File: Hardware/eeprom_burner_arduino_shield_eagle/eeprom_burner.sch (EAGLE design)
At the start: 5 parts, among them IC2 74LS595N, IC3 74LS595N

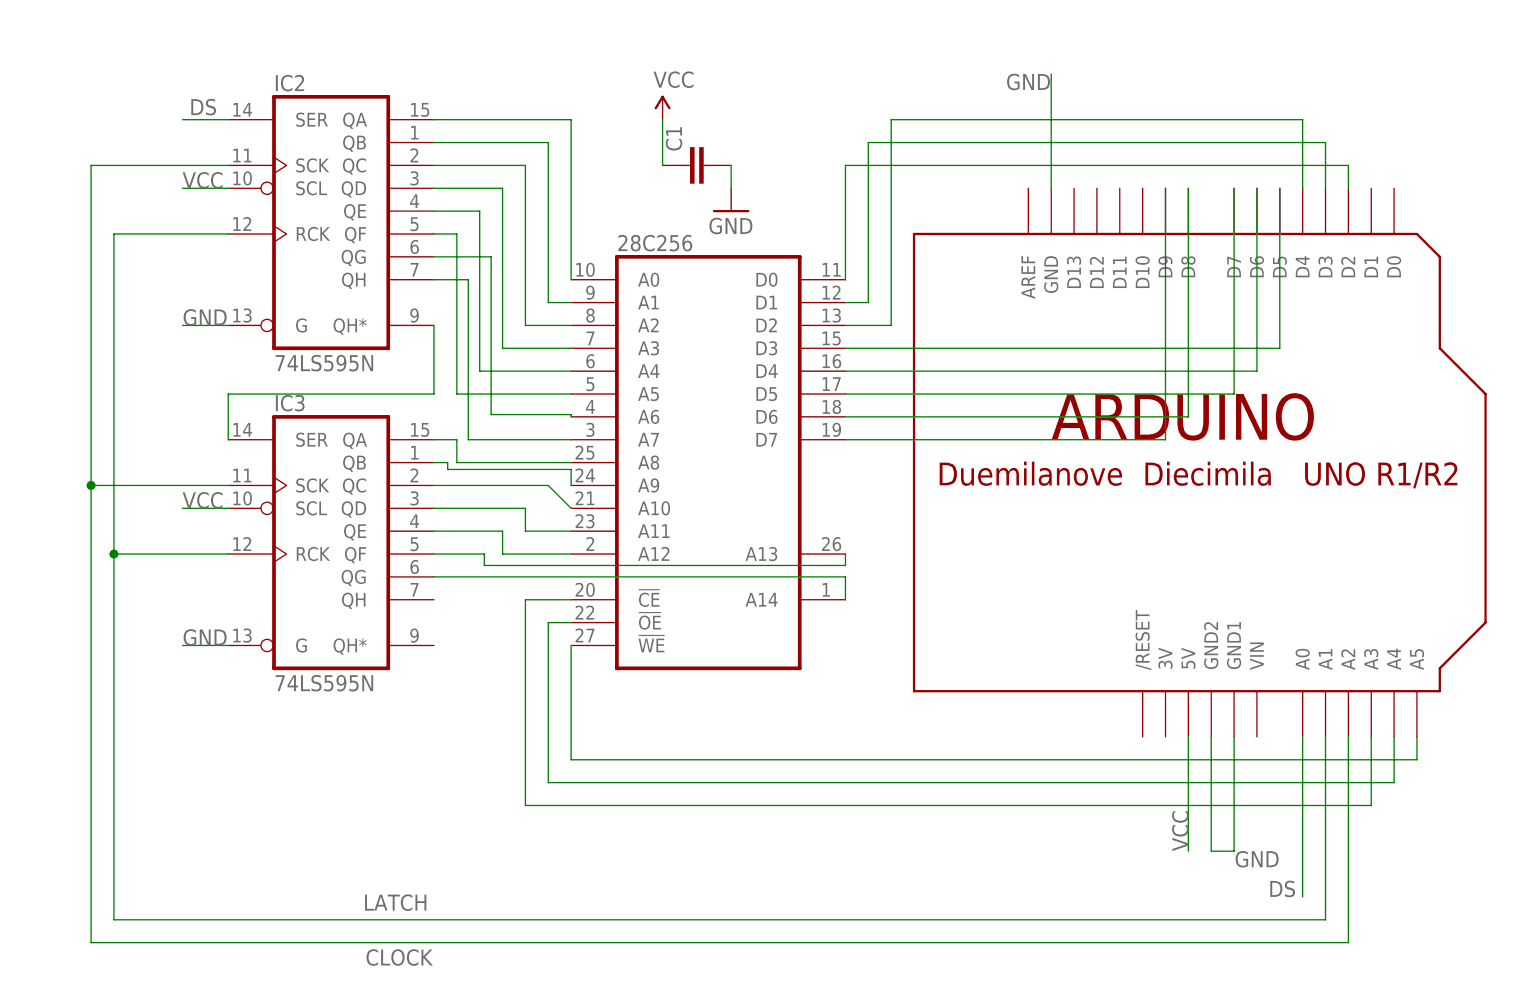
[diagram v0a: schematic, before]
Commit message: Python CLI, Paged Write, Unlocker
Fleshed out python command line interface
Added paged write and unlock functions
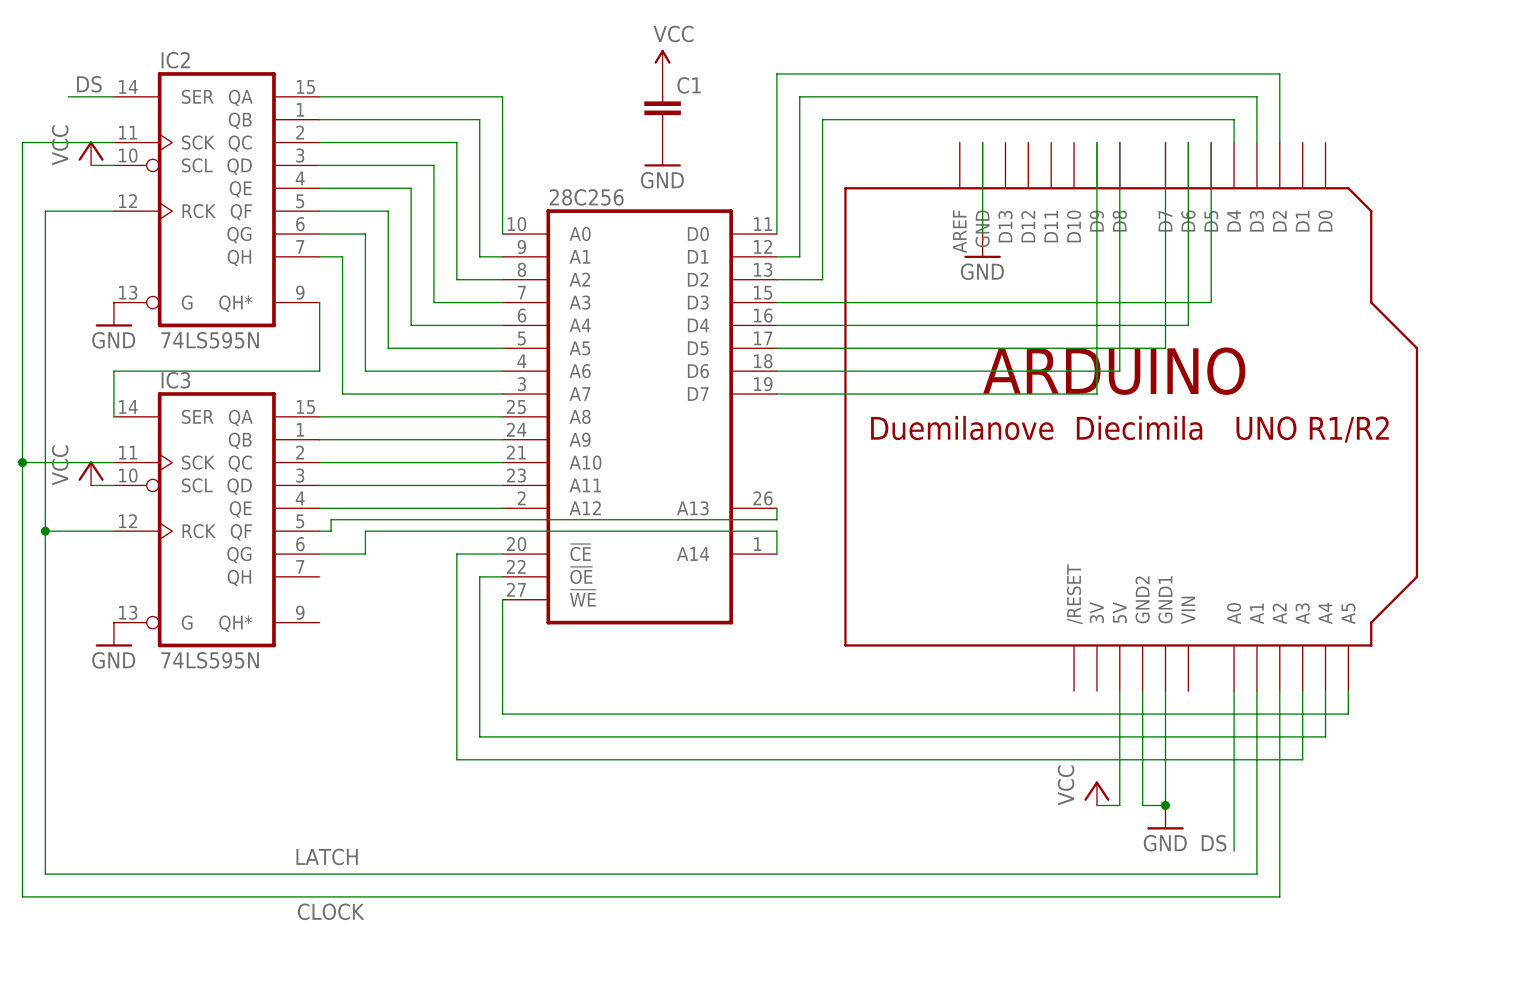
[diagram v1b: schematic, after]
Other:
- moved on the sheet: 28C256, C1, IC2, IC3
